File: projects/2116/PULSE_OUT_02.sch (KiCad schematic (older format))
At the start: 52 parts, among them CN10 HIF3FC-16PA-2.54DSA, CN11 HIF3FC-16PA-2.54DSA, CN8 HIF3FC-16PA-2.54DS, CN9 HIF3FC-16PA-2.54DS, IC32 74HCT574, IC33 74HCT574, IC34 74HCT574, IC35 74HCT574, IC36 74HCT541, IC37 74HCT541, IC38 74HCT541, IC39 74HCT541

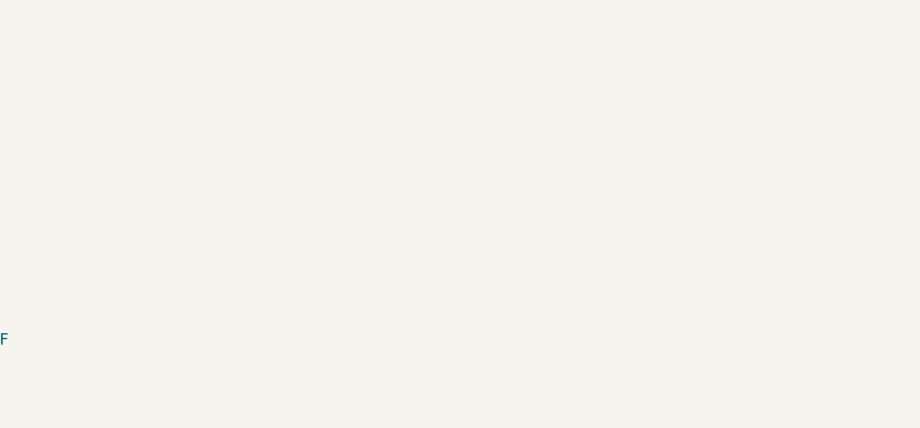
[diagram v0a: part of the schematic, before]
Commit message: 基板端に電源コネクタを追加。
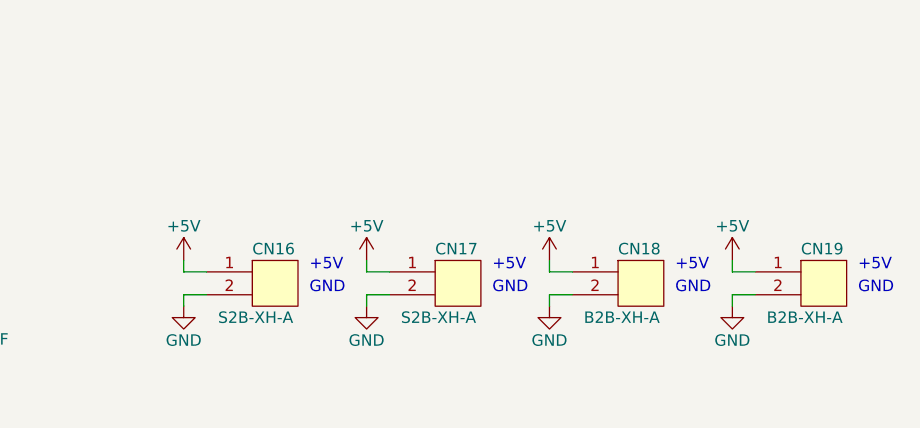
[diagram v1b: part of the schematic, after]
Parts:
- added CN16, CN17: S2B-XH-A, A01myFootPrint:S2B-XH-A, symbol connectors:2PIN
- added CN18, CN19: B2B-XH-A, A01myFootPrint:cn_B2B-XH-A, symbol connectors:2PIN
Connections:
- wire segments 324 -> 340
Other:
- note added: "+5V"
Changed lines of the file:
@@
 Text Label 4600 1600 0    50   ~ 0
 Q23
+$Comp
+L connectors:2PIN CN?
+U 1 1 61CA2F87
+P 7450 6200
+AR Path="/61AA6AFE/61CA2F87" Ref="CN?"  Part="1"
+AR Path="/61F79E7A/61CA2F87" Ref="CN16"  Part="1"
+F 0 "CN16" H 7350 6350 50  0000 L CNN
+F 1 "S2B-XH-A" H 7200 6050 50  0000 L CNN
+F 2 "A01myFootPrint:S2B-XH-A" H 7450 6200 60  0001 C CNN
+F 3 "" H 7450 6200 60  0001 C CNN
+	1    7450 6200
+	1    0    0    -1
+$EndComp
+$Comp
+L power:GND #PWR?
+U 1 1 61CA2F8D
+P 7050 6300
+AR Path="/61CA2F8D" Ref="#PWR?"  Part="1"
+AR Path="/61BC7329/61CA2F8D" Ref="#PWR?"  Part="1"
+AR Path="/61AA6AFE/61CA2F8D" Ref="#PWR?"  Part="1"
+AR Path="/61F79E7A/61CA2F8D" Ref="#PWR0216"  Part="1"
+F 0 "#PWR0216" H 7050 6050 50  0001 C CNN
+F 1 "GND" H 7050 6150 50  0000 C CNN
+F 2 "" H 7050 6300 50  0001 C CNN
+F 3 "" H 7050 6300 50  0001 C CNN
+	1    7050 6300
+	1    0    0    -1
+$EndComp
+$Comp
+L power:+5V #PWR?
+U 1 1 61CA2F93
+P 7050 6100
+AR Path="/61CA2F93" Ref="#PWR?"  Part="1"
+AR Path="/61BC7329/61CA2F93" Ref="#PWR?"  Part="1"
+AR Path="/61AA6AFE/61CA2F93" Ref="#PWR?"  Part="1"
+AR Path="/61F79E7A/61CA2F93" Ref="#PWR0215"  Part="1"
+F 0 "#PWR0215" H 7050 5950 50  0001 C CNN
+F 1 "+5V" H 7050 6250 50  0000 C CNN
+F 2 "" H 7050 6100 50  0001 C CNN
+F 3 "" H 7050 6100 50  0001 C CNN
+	1    7050 6100
+	1    0    0    -1
+$EndComp
+Wire Wire Line
+	7150 6150 7050 6150
+Wire Wire Line
+	7050 6150 7050 6100
+Wire Wire Line
+	7150 6250 7050 6250
+Wire Wire Line
+	7050 6250 7050 6300
+Text Notes 7600 6250 0    50   ~ 0
+GND
+Text Notes 7600 6150 0    50   ~ 0
++5V
+$Comp
+L connectors:2PIN CN?
+U 1 1 61CA2F9F
+P 8250 6200
+AR Path="/61AA6AFE/61CA2F9F" Ref="CN?"  Part="1"
+AR Path="/61F79E7A/61CA2F9F" Ref="CN17"  Part="1"
+F 0 "CN17" H 8150 6350 50  0000 L CNN
+F 1 "S2B-XH-A" H 8000 6050 50  0000 L CNN
+F 2 "A01myFootPrint:S2B-XH-A" H 8250 6200 60  0001 C CNN
+F 3 "" H 8250 6200 60  0001 C CNN
+	1    8250 6200
+	1    0    0    -1
+$EndComp
+$Comp
+L power:GND #PWR?
+U 1 1 61CA2FA5
+P 7850 6300
+AR Path="/61CA2FA5" Ref="#PWR?"  Part="1"
+AR Path="/61BC7329/61CA2FA5" Ref="#PWR?"  Part="1"
+AR Path="/61AA6AFE/61CA2FA5" Ref="#PWR?"  Part="1"
+AR Path="/61F79E7A/61CA2FA5" Ref="#PWR0218"  Part="1"
+F 0 "#PWR0218" H 7850 6050 50  0001 C CNN
+F 1 "GND" H 7850 6150 50  0000 C CNN
+F 2 "" H 7850 6300 50  0001 C CNN
+F 3 "" H 7850 6300 50  0001 C CNN
+	1    7850 6300
+	1    0    0    -1
+$EndComp
+$Comp
+L power:+5V #PWR?
+U 1 1 61CA2FAB
+P 7850 6100
+AR Path="/61CA2FAB" Ref="#PWR?"  Part="1"
+AR Path="/61BC7329/61CA2FAB" Ref="#PWR?"  Part="1"
+AR Path="/61AA6AFE/61CA2FAB" Ref="#PWR?"  Part="1"
+AR Path="/61F79E7A/61CA2FAB" Ref="#PWR0217"  Part="1"
+F 0 "#PWR0217" H 7850 5950 50  0001 C CNN
+F 1 "+5V" H 7850 6250 50  0000 C CNN
+F 2 "" H 7850 6100 50  0001 C CNN
+F 3 "" H 7850 6100 50  0001 C CNN
+	1    7850 6100
+	1    0    0    -1
+$EndComp
+Wire Wire Line
+	7950 6150 7850 6150
+Wire Wire Line
+	7850 6150 7850 6100
+Wire Wire Line
+	7950 6250 7850 6250
+Wire Wire Line
+	7850 6250 7850 6300
+Text Notes 8400 6250 0    50   ~ 0
+GND
+Text Notes 8400 6150 0    50   ~ 0
++5V
+$Comp
+L connectors:2PIN CN?
+U 1 1 61CA2FB7
+P 9050 6200
+AR Path="/61AA6AFE/61CA2FB7" Ref="CN?"  Part="1"
+AR Path="/61F79E7A/61CA2FB7" Ref="CN18"  Part="1"
+F 0 "CN18" H 8950 6350 50  0000 L CNN
+F 1 "B2B-XH-A" H 8800 6050 50  0000 L CNN
+F 2 "A01myFootPrint:cn_B2B-XH-A" H 9050 6200 60  0001 C CNN
+F 3 "" H 9050 6200 60  0001 C CNN
+	1    9050 6200
+	1    0    0    -1
+$EndComp
+$Comp
+L power:GND #PWR?
+U 1 1 61CA2FBD
+P 8650 6300
+AR Path="/61CA2FBD" Ref="#PWR?"  Part="1"
+AR Path="/61BC7329/61CA2FBD" Ref="#PWR?"  Part="1"
+AR Path="/61AA6AFE/61CA2FBD" Ref="#PWR?"  Part="1"
+AR Path="/61F79E7A/61CA2FBD" Ref="#PWR0220"  Part="1"
+F 0 "#PWR0220" H 8650 6050 50  0001 C CNN
+F 1 "GND" H 8650 6150 50  0000 C CNN
+F 2 "" H 8650 6300 50  0001 C CNN
+F 3 "" H 8650 6300 50  0001 C CNN
+	1    8650 6300
+	1    0    0    -1
+$EndComp
+$Comp
+L power:+5V #PWR?
+U 1 1 61CA2FC3
+P 8650 6100
+AR Path="/61CA2FC3" Ref="#PWR?"  Part="1"
+AR Path="/61BC7329/61CA2FC3" Ref="#PWR?"  Part="1"
+AR Path="/61AA6AFE/61CA2FC3" Ref="#PWR?"  Part="1"
+AR Path="/61F79E7A/61CA2FC3" Ref="#PWR0219"  Part="1"
+F 0 "#PWR0219" H 8650 5950 50  0001 C CNN
+F 1 "+5V" H 8650 6250 50  0000 C CNN
+F 2 "" H 8650 6100 50  0001 C CNN
+F 3 "" H 8650 6100 50  0001 C CNN
+	1    8650 6100
+	1    0    0    -1
+$EndComp
+Wire Wire Line
+	8750 6150 8650 6150
+Wire Wire Line
+	8650 6150 8650 6100
+Wire Wire Line
+	8750 6250 8650 6250
+Wire Wire Line
+	8650 6250 8650 6300
+Text Notes 9200 6250 0    50   ~ 0
+GND
+Text Notes 9200 6150 0    50   ~ 0
++5V
+$Comp
+L connectors:2PIN CN?
+U 1 1 61CA2FCF
+P 9850 6200
+AR Path="/61AA6AFE/61CA2FCF" Ref="CN?"  Part="1"
+AR Path="/61F79E7A/61CA2FCF" Ref="CN19"  Part="1"
+F 0 "CN19" H 9750 6350 50  0000 L CNN
+F 1 "B2B-XH-A" H 9600 6050 50  0000 L CNN
+F 2 "A01myFootPrint:cn_B2B-XH-A" H 9850 6200 60  0001 C CNN
+F 3 "" H 9850 6200 60  0001 C CNN
+	1    9850 6200
+	1    0    0    -1
+$EndComp
+$Comp
+L power:GND #PWR?
+U 1 1 61CA2FD5
+P 9450 6300
+AR Path="/61CA2FD5" Ref="#PWR?"  Part="1"
+AR Path="/61BC7329/61CA2FD5" Ref="#PWR?"  Part="1"
+AR Path="/61AA6AFE/61CA2FD5" Ref="#PWR?"  Part="1"
+AR Path="/61F79E7A/61CA2FD5" Ref="#PWR0222"  Part="1"
+F 0 "#PWR0222" H 9450 6050 50  0001 C CNN
+F 1 "GND" H 9450 6150 50  0000 C CNN
+F 2 "" H 9450 6300 50  0001 C CNN
+F 3 "" H 9450 6300 50  0001 C CNN
+	1    9450 6300
+	1    0    0    -1
+$EndComp
+$Comp
+L power:+5V #PWR?
+U 1 1 61CA2FDB
+P 9450 6100
+AR Path="/61CA2FDB" Ref="#PWR?"  Part="1"
+AR Path="/61BC7329/61CA2FDB" Ref="#PWR?"  Part="1"
+AR Path="/61AA6AFE/61CA2FDB" Ref="#PWR?"  Part="1"
+AR Path="/61F79E7A/61CA2FDB" Ref="#PWR0221"  Part="1"
+F 0 "#PWR0221" H 9450 5950 50  0001 C CNN
+F 1 "+5V" H 9450 6250 50  0000 C CNN
+F 2 "" H 9450 6100 50  0001 C CNN
+F 3 "" H 9450 6100 50  0001 C CNN
+	1    9450 6100
+	1    0    0    -1
+$EndComp
+Wire Wire Line
+	9550 6150 9450 6150
+Wire Wire Line
+	9450 6150 9450 6100
+Wire Wire Line
+	9550 6250 9450 6250
+Wire Wire Line
+	9450 6250 9450 6300
+Text Notes 10000 6250 0    50   ~ 0
+GND
+Text Notes 10000 6150 0    50   ~ 0
++5V
 $EndSCHEMATC
